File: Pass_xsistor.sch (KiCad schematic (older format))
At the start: 4 parts

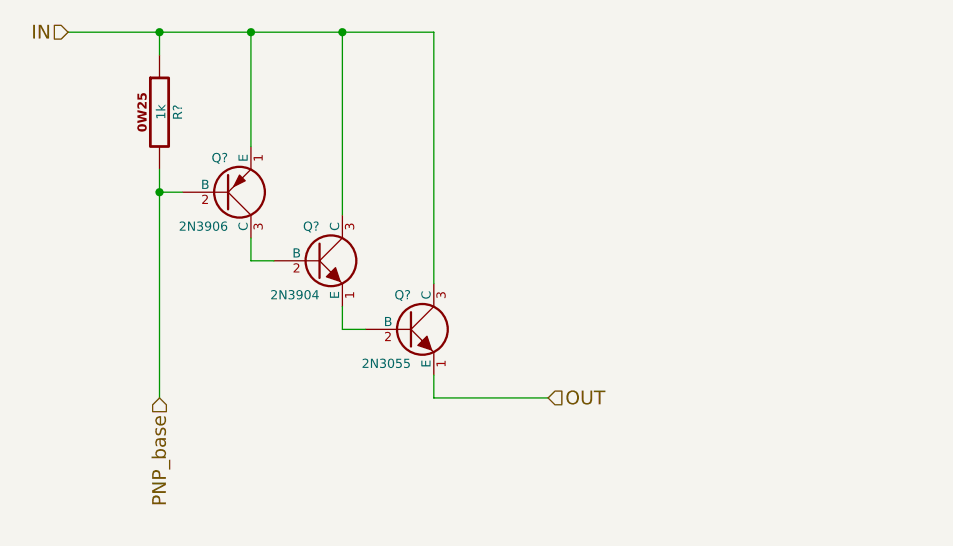
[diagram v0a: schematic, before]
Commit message: adding base resistor to pnp.
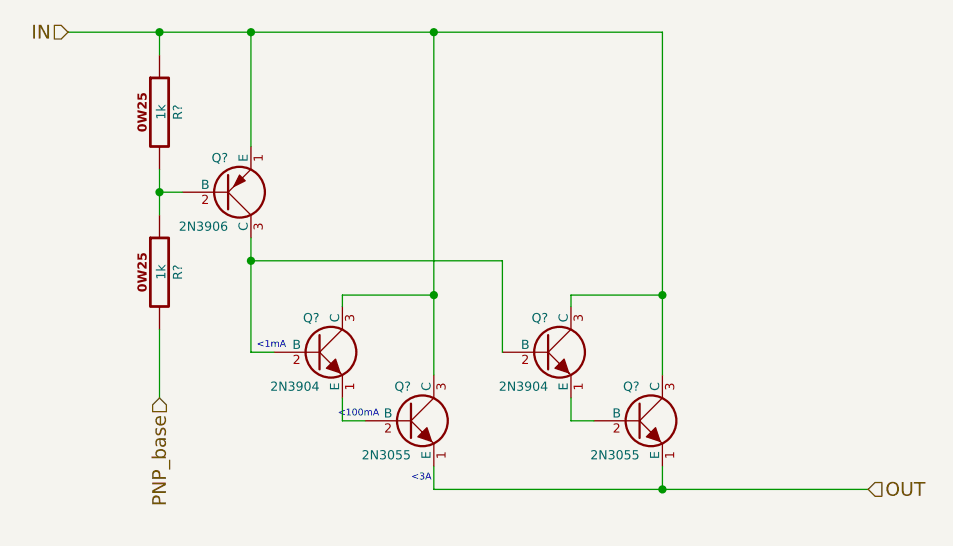
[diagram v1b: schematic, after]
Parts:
- added Q?: 2N3904, ~, symbol 2N3904
- added Q?: 2N3055, ~, symbol NPN_EBC
- added R?: 1k, ~, symbol R_0W25
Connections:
- net IN: now also Q?.3 (C), Q?.3 (C)
- net OUT: now also Q?.1 (E)
- net PNP_base: now also R?.2; no longer Q?.2 (B), R?.2
- net at Q?.2 (B), Q?.3 (C): now also Q?.2 (B)
- new net: Q?.2 (B), R?.1, R?.2
- new net: Q?.1 (E), Q?.2 (B)
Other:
- note added: "<100mA"
- note added: "<1mA"
- note added: "<3A"
- moved on the sheet: Q?
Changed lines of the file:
@@
 $EndDescr
 Wire Wire Line
-	5950 2750 5950 3550
-Wire Wire Line
-	5650 3750 5550 3750
-Wire Wire Line
-	5550 3750 5550 3650
+	5550 3650 5550 4150
 Wire Wire Line
 	5550 2750 5550 3250
@@
 $EndComp
 Wire Wire Line
-	4750 2750 6350 2750
+	4750 2750 7350 2750
 Connection ~ 5550 2750
 Wire Wire Line
@@
 L NPN_EBC Q?
 U 1 1 53385B4D
-P 6250 4050
-F 0 "Q?" H 6250 4200 40  0000 R CNN
-F 1 "2N3055" H 6250 3900 40  0000 R CNN
-F 2 "~" H 6250 4050 60  0000 C CNN
-F 3 "~" H 6250 4050 60  0000 C CNN
-	1    6250 4050
+P 6250 4450
+F 0 "Q?" H 6250 4600 40  0000 R CNN
+F 1 "2N3055" H 6250 4300 40  0000 R CNN
+F 2 "~" H 6250 4450 60  0000 C CNN
+F 3 "~" H 6250 4450 60  0000 C CNN
+	1    6250 4450
 	1    0    0    -1
 $EndComp
-Connection ~ 5950 2750
 $Comp
 L 2N3904 Q?
 U 1 1 53385B6C
-P 5850 3750
-F 0 "Q?" H 5850 3900 40  0000 R CNN
-F 1 "2N3904" H 5850 3600 40  0000 R CNN
-F 2 "~" H 5850 3750 60  0000 C CNN
-F 3 "~" H 5850 3750 60  0000 C CNN
-	1    5850 3750
+P 5850 4150
+F 0 "Q?" H 5850 4300 40  0000 R CNN
+F 1 "2N3904" H 5850 4000 40  0000 R CNN
+F 2 "~" H 5850 4150 60  0000 C CNN
+F 3 "~" H 5850 4150 60  0000 C CNN
+	1    5850 4150
 	1    0    0    -1
 $EndComp
@@
 $EndComp
 Wire Wire Line
-	5950 3950 5950 4050
+	5950 4350 5950 4450
 Wire Wire Line
-	5950 4050 6050 4050
+	5950 4450 6050 4450
 Wire Wire Line
-	6350 2750 6350 3850
+	6350 2750 6350 4250
 Text HLabel 4750 2750 0    60   Input ~ 0
 IN
-Text HLabel 6850 4350 2    60   Input ~ 0
+Text HLabel 8250 4750 2    60   Input ~ 0
 OUT
 Wire Wire Line
-	6350 4250 6350 4350
+	6350 4650 6350 4750
 Wire Wire Line
-	6350 4350 6850 4350
-Wire Wire Line
-	5150 3350 5150 4350
+	6350 4750 8250 4750
 Text HLabel 5150 4350 3    60   Input ~ 0
 PNP_base
+$Comp
+L 2N3904 Q?
+U 1 1 533AB457
+P 6850 4150
+F 0 "Q?" H 6850 4300 40  0000 R CNN
+F 1 "2N3904" H 6850 4000 40  0000 R CNN
+F 2 "~" H 6850 4150 60  0000 C CNN
+F 3 "~" H 6850 4150 60  0000 C CNN
+	1    6850 4150
+	1    0    0    -1
+$EndComp
+$Comp
+L NPN_EBC Q?
+U 1 1 533AB45D
+P 7250 4450
+F 0 "Q?" H 7250 4600 40  0000 R CNN
+F 1 "2N3055" H 7250 4300 40  0000 R CNN
+F 2 "~" H 7250 4450 60  0000 C CNN
+F 3 "~" H 7250 4450 60  0000 C CNN
+	1    7250 4450
+	1    0    0    -1
+$EndComp
+Wire Wire Line
+	6950 4350 6950 4450
+Wire Wire Line
+	6950 4450 7050 4450
+Connection ~ 6350 2750
+Wire Wire Line
+	7350 2750 7350 4250
+Wire Wire Line
+	7350 4650 7350 4750
+Connection ~ 7350 4750
+Wire Wire Line
+	5550 4150 5650 4150
+Wire Wire Line
+	5550 3750 6650 3750
+Wire Wire Line
+	6650 3750 6650 4150
+Connection ~ 5550 3750
+Text Notes 6340 4720 2    30   ~ 0
+<3A
+Text Notes 5930 4440 0    30   ~ 0
+<100mA
+Text Notes 5575 4140 0    30   ~ 0
+<1mA
+Wire Wire Line
+	5950 3950 5950 3900
+Wire Wire Line
+	5950 3900 6350 3900
+Connection ~ 6350 3900
+Wire Wire Line
+	6950 3950 6950 3900
+Wire Wire Line
+	6950 3900 7350 3900
+Connection ~ 7350 3900
+$Comp
+L R_0W25 R?
+U 1 1 533B4F14
+P 5150 3800
+F 0 "R?" V 5230 3800 40  0000 C CNN
+F 1 "1k" V 5157 3801 40  0000 C CNN
+F 2 "~" V 5080 3800 30  0000 C CNN
+F 3 "~" H 5150 3800 30  0000 C CNN
+	1    5150 3800
+	1    0    0    -1
+$EndComp
+Wire Wire Line
+	5150 3350 5150 3550
+Wire Wire Line
+	5150 4050 5150 4350
 $EndSCHEMATC
